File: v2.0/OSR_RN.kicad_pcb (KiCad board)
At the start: 2 copper layers, 63.5 x 43 mm, 76 parts, among them J1 U.FL, J2 I2C, J3 ISP_ATM, J4 ISP_RN, J5 UART, J6 OUT, J7 BAT1, J8 SOL1, J9 USB_B_Micro, Q1 YJL2301F, Q2 BC817, SW1 RESET, U1 ATmega328-AU, U2 CH340E, U3 AP2112K-3.3, U4 MCP73831-2-OT, U5 RN2483, Y1 16MHz

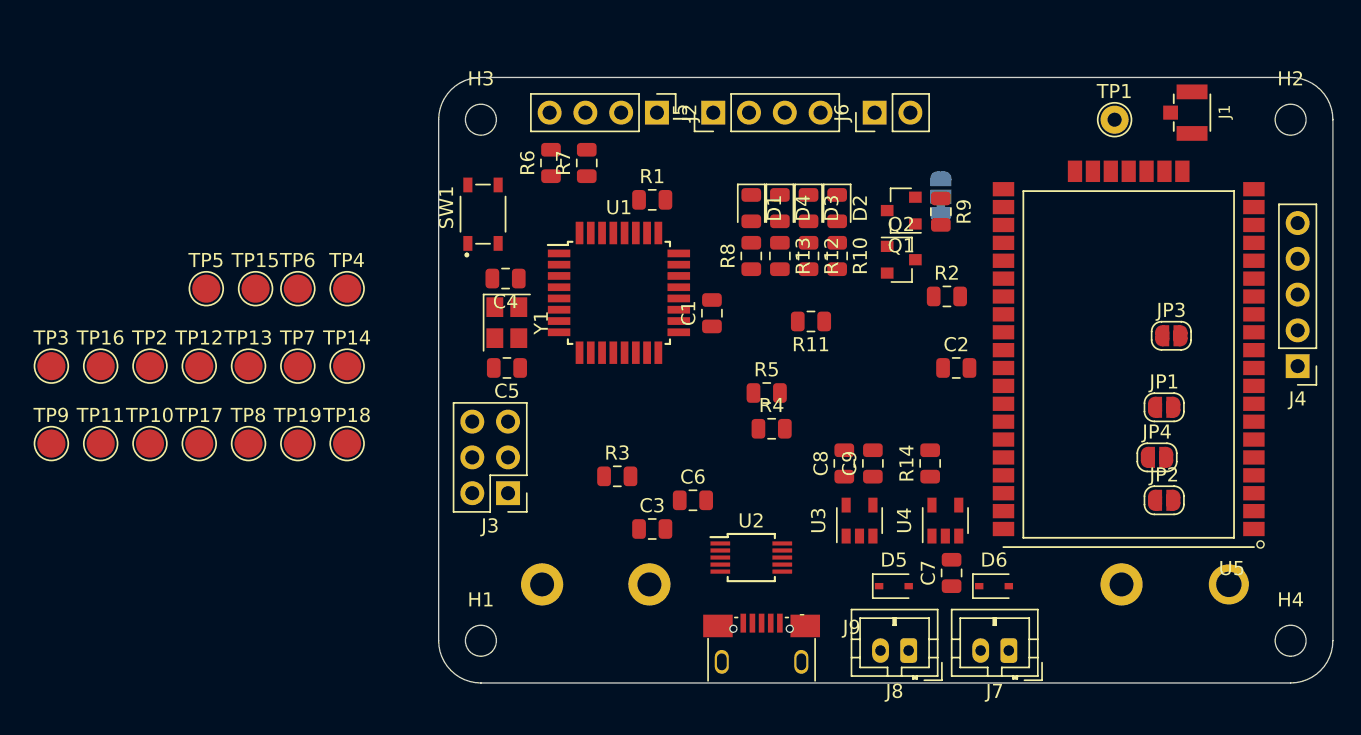
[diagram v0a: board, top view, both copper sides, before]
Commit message: -Zmiany w schemacie: 	-Usunięte połączenia z RN do header'ów, zastąpione TestPoint'ami -Aktualizacja projektu płytki
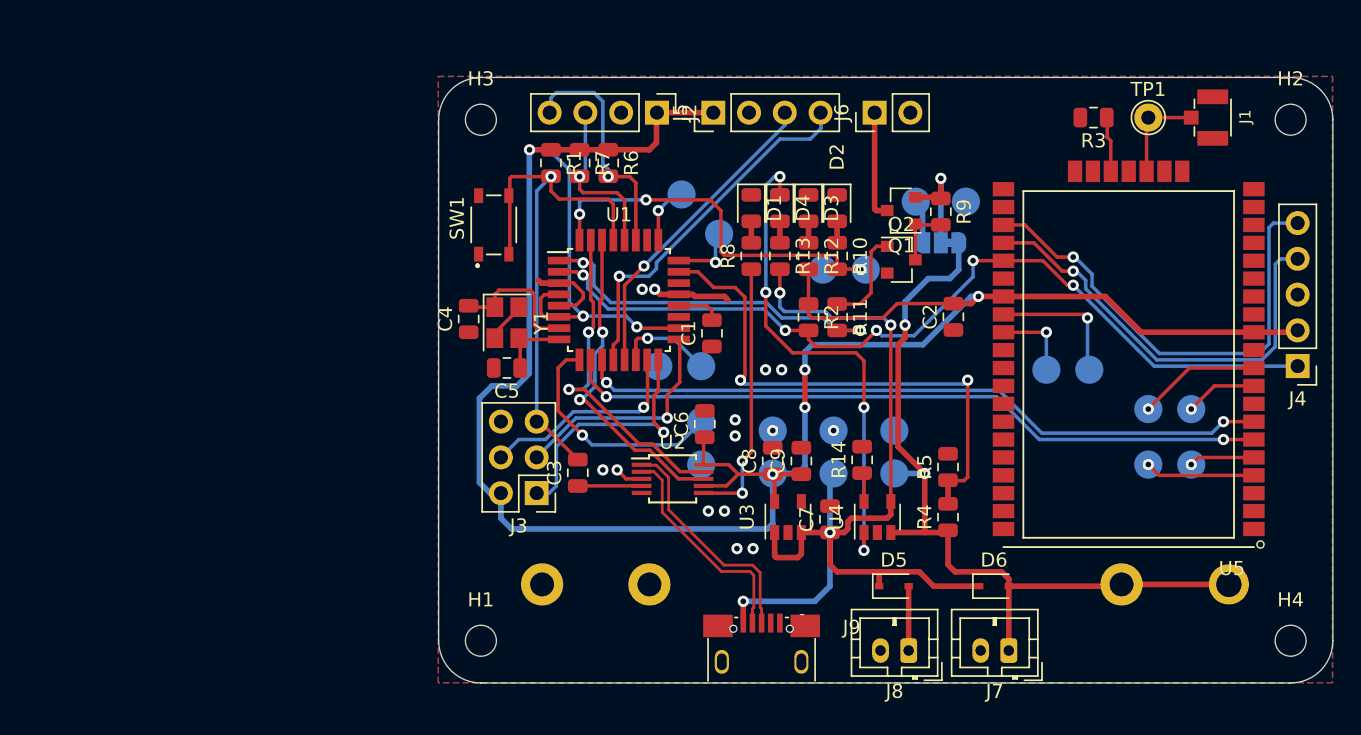
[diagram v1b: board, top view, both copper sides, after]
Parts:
- removed JP1, JP2: RN_LED, Jumper:SolderJumper-2_P1.3mm_Open_RoundedPad1.0x1.5mm
- removed JP3: RX, Jumper:SolderJumper-2_P1.3mm_Open_RoundedPad1.0x1.5mm
- removed JP4: TX, Jumper:SolderJumper-2_P1.3mm_Open_RoundedPad1.0x1.5mm
- added TP20: RN_SDA, TestPoint:TestPoint_Pad_D2.0mm, B.Cu at (167.9, 94.5)
- added TP21: RN_SCL, TestPoint:TestPoint_Pad_D2.0mm, B.Cu at (170.9, 94.5)
- added TP22: RN_RX, TestPoint:TestPoint_Pad_D2.0mm, B.Cu at (167.9, 90.6)
- added TP23: RN_TX, TestPoint:TestPoint_Pad_D2.0mm, B.Cu at (170.9, 90.6)
- TP10, TP11, TP12, TP13, TP14, TP15, TP16, TP17, TP18, TP19, TP2, TP3, TP4, TP5, TP6, TP7, TP8, TP9: moved to B.Cu
- moved TP3 70.7 mm to (160.7, 87.8)
- moved TP2 66.7 mm to (163.7, 87.8)
- moved TP17 57.1 mm to (154.9, 75.8)
- moved TP11 56.4 mm to (149.9, 92.1)
- moved TP9 55.5 mm to (145.5, 92.1)
- moved TP16 54.8 mm to (147.8, 80.6)
- moved TP15 47.3 mm to (151.4, 75.8)
- moved TP5 46.4 mm to (145.5, 95.1)
- moved TP10 44.2 mm to (141.2, 92.1)
- moved R3 42.3 mm to (164.0, 69.8), turned to 180 degrees
- moved TP4 41.0 mm to (149.9, 95.1)
- moved TP19 39.3 mm to (144.8, 80.6)
- moved TP6 36.2 mm to (141.2, 95.1)
- moved TP12 35.9 mm to (136.1, 91.4)
- moved TP13 32.1 mm to (136.1, 87.5)
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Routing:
- net VCC: track 0.00 -> 173.9 mm, vias 0 -> 7
- net VBUS: track 0.00 -> 67.7 mm, vias 0 -> 4
- net D4\RST_RN: track 0.00 -> 61.8 mm, vias 0 -> 5
- net +BATT: track 0.00 -> 58.4 mm, vias 0 -> 2
- net D6\RN_TX: track 0.00 -> 50.3 mm, vias 0 -> 2
- net D7\RN_RX: track 0.00 -> 49.5 mm, vias 0 -> 2
- net RST: track 0.00 -> 38.5 mm, vias 0 -> 1
- net A0: track 0.00 -> 38.0 mm, vias 0 -> 2
- net Net-(D4-Pad1): track 0.00 -> 35.1 mm, vias 0 -> 4
- net PGC_INT: track 0.00 -> 33.8 mm, vias 0 -> 1
- net PGD_INT: track 0.00 -> 31.1 mm, vias 0 -> 1
- net D2\LED: track 0.00 -> 27.0 mm, vias 0 -> 3
- net D8\Rx: track 0.00 -> 26.1 mm, vias 0 -> 1
- net D3\MOSFET: track 0.00 -> 25.9 mm, vias 0 -> 2
- net TxD: track 0.00 -> 23.9 mm, vias 0 -> 2
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- added copper zone on B.Cu, net GND
- added copper zone on F.Cu, net GND

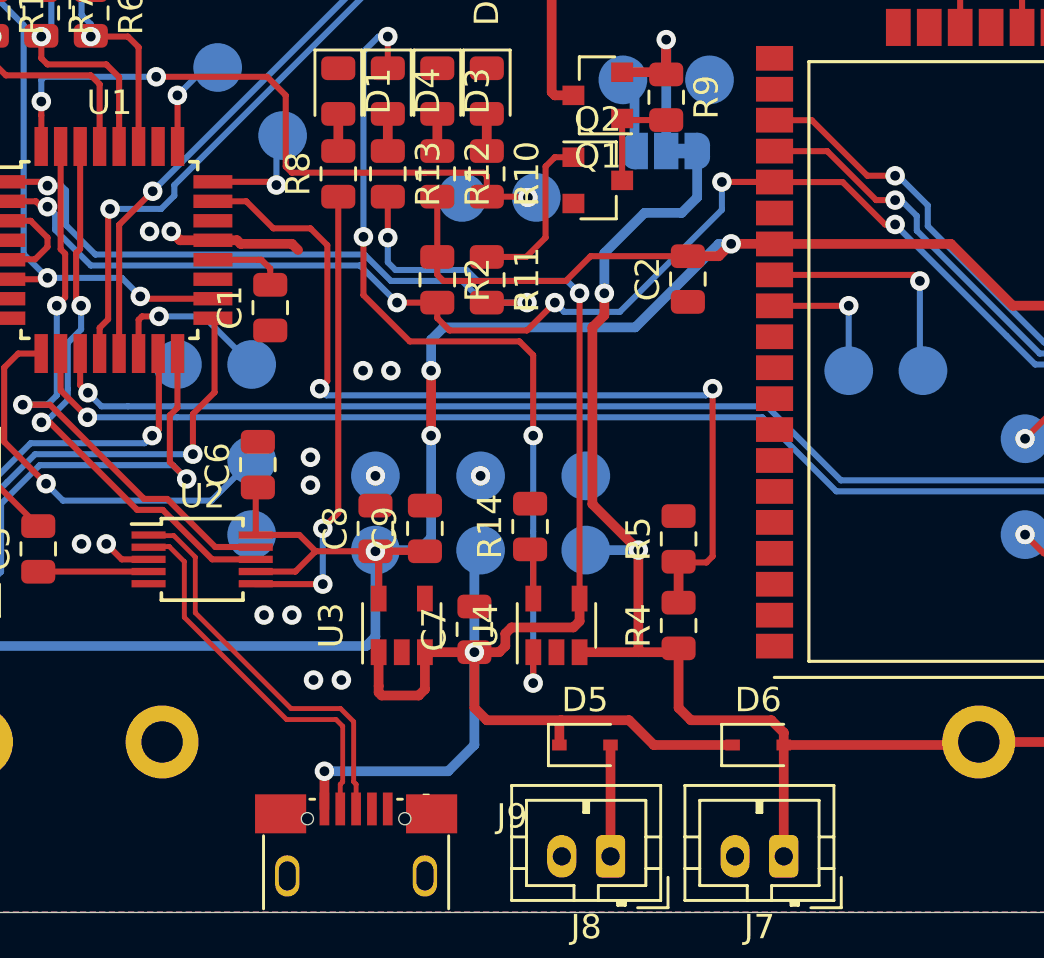
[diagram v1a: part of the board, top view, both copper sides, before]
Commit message: Przeorganizowanie ścieżek.
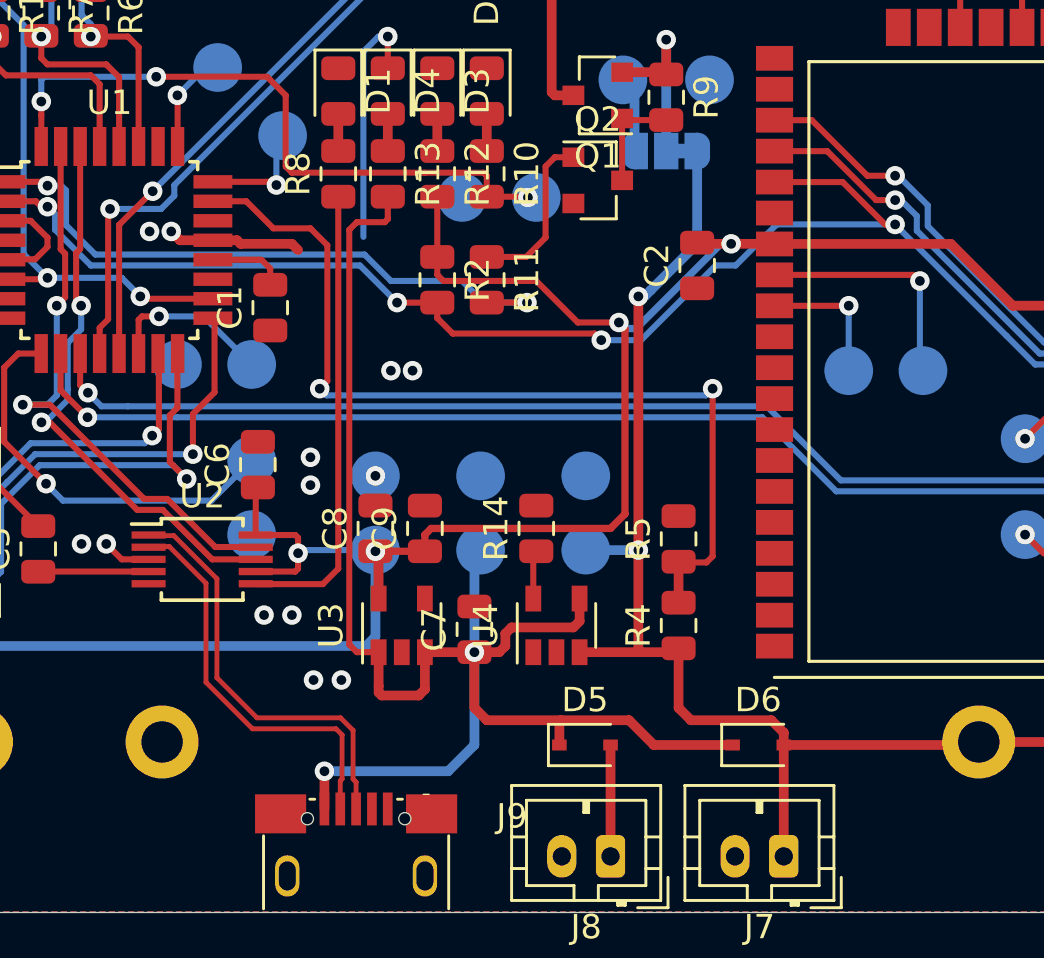
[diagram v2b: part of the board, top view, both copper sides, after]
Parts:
- moved C2 0.67 mm to (154.4, 83.4)
- moved R14 0.27 mm to (147.8, 94.2)
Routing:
- net Net-(D4-Pad1): track 35.1 -> 10.0 mm, vias 4 -> 1
- net D4\RST_RN: track 61.8 -> 65.4 mm, vias 5 -> 4
- net VCC: track 173.9 -> 170.4 mm
- net VBUS: track 67.7 -> 65.1 mm, vias 4 -> 2
- net +BATT: track 58.4 -> 56.1 mm
- net D+: track 16.6 -> 17.4 mm
- net D-: track 15.8 -> 16.6 mm
- net Net-(R8-Pad1): vias 2 -> 0
- net GND: vias 14 -> 13

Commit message: 90%
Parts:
- removed J1: U.FL, U.FL-R-SMT-1_10_:HRS_U.FL-R-SMT-1(10)
- removed J7: BAT1, Connector_JST:JST_PH_B2B-PH-K_1x02_P2.00mm_Vertical
- removed J8: SOL1, Connector_JST:JST_PH_B2B-PH-K_1x02_P2.00mm_Vertical
- removed J9: USB_B_Micro, OSR_BOARD:micro_usb
- added ANT: U.FL, OSR_BOARD:HRS_U.FL-R-SMT-1(10), F.Cu at (172.5, 69.8)
- added BATTERY: BAT1, Connector_JST:JST_PH_S2B-PH-K_1x02_P2.00mm_Horizontal, F.Cu at (158.1, 103.5)
- added PV: SOL1, Connector_JST:JST_PH_S2B-PH-K_1x02_P2.00mm_Horizontal, F.Cu at (151.1, 103.5)
- added Ref**: Val**, OSR_BOARD:OSR_Horizontal_12x29, B.Cu at (160.9, 79.6)
- added USB: USB_B_Micro, OSR_BOARD:WE_629105136821, F.Cu at (140.4, 108.2)
- moved D6 9.97 mm to (147.1, 104.5)
- moved GND 6.10 mm to (139.2, 87.5)
- moved A1 4.87 mm to (136.1, 73.4)
- moved D5 3.75 mm to (136.1, 95.2)
- moved D5 2.81 mm to (147.1, 102.6)
- moved TP7 2.52 mm to (133.1, 73.4)
- moved A_IN 2.41 mm to (163.7, 90.2)
- moved D_OUT 2.41 mm to (160.7, 90.2)
- moved GND 2.41 mm to (136.1, 92.1)
- moved RX 1.09 mm to (166.9, 90.2)
- moved TX 1.09 mm to (169.9, 90.2)
- moved Q1 0.06 mm to (150.4, 76.4)
- renumbered TP14 to A1, J3 to ATM_ISP, TP2 to A_IN, TP13 to D10, TP16 to D2/LED, TP12 to D5, TP3 to D_OUT, TP8 to GND, TP17 to GND, TP18 to GND, TP19 to GND, J2 to I2C, J6 to OUT, SW1 to RESET, U5 to RN2483, J4 to RN_ISP, TP22 to RX, TP21 to SCL, TP20 to SDA, TP23 to TX, J5 to UART, TP5 to VBUS, TP6 to VCC, TP4 to V_BAT, TP15 to V_EXT
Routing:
- net Net-(D4-Pad1): track 10.0 -> 42.5 mm, vias 1 -> 4
- net VBUS: track 65.1 -> 56.1 mm
- net +BATT: track 56.1 -> 64.4 mm
- net VCC: track 170.4 -> 162.8 mm
- net GND: track 16.2 -> 20.6 mm, vias 13 -> 18
- net A1: track 4.44 -> 7.41 mm
- net RST: track 38.5 -> 36.0 mm, vias 1 -> 2
- net A0: track 38.0 -> 39.8 mm
- net A2: track 3.72 -> 5.40 mm
- net Net-(TP3-Pad1): track 5.84 -> 7.25 mm
- net Net-(TP22-Pad1): track 8.70 -> 10.0 mm
- net Net-(D5-Pad2): track 4.57 -> 3.42 mm
- net D2\LED: track 27.0 -> 28.1 mm
- net PGD_INT: track 31.1 -> 32.1 mm
- net Net-(TP23-Pad1): track 5.13 -> 5.99 mm
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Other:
- board text added: "LoRa Dev Board v2"
- board text added: "RN_2483"
- board text added: "VCC"
- board text added: "WWW.OTWARTASIECRZECZY.ORG"

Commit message: 95%
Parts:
- moved Ref** 4.61 mm to (162.7, 83.8), turned to 180 degrees
- renumbered TP7 to A2, D4 to CHG, D2 to LED, D1 to USB, D3 to VCC

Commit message: SCH: -kosmetyka PCB: -Zmiana złącz baterii i panelu fotowoltaicznego na raster 2.5mm (JST). -Zmiana obudowy diod zabezpieczających. -Kosmetyka
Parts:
- D5, D6: footprint Diode_SMD:D_SOD-323 -> Diode_SMD:D_SOD-123
- TP2: renamed from A_IN; value RN_ANALOG_IN -> A_IN
- TP3: renamed from D_OUT; value LED -> D_OUT
- moved D6 18.1 mm to (165.1, 106.6)
- moved D5 1.45 mm to (147.4, 104.0), turned to 90 degrees
- renumbered USB to D1, LED to D2, VCC to D3, CHG to D4, ANT to J1, I2C to J2, ATM_ISP to J3, RN_ISP to J4, UART to J5, OUT to J6, BATTERY to J7, PV to J8, USB to J9, RESET to SW1, D5 to TP12, D10 to TP13, A1 to TP14, V_EXT to TP15, D2/LED to TP16, GND to TP17, GND to TP18, GND to TP19, SDA to TP20, SCL to TP21, RX to TP22, TX to TP23, V_BAT to TP4, VBUS to TP5, VCC to TP6, A2 to TP7, GND to TP8, RN2483 to U5
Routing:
- net VBUS: track 56.1 -> 74.9 mm
- net +BATT: track 64.4 -> 57.0 mm
- net Net-(D5-Pad2): track 3.42 -> 4.28 mm

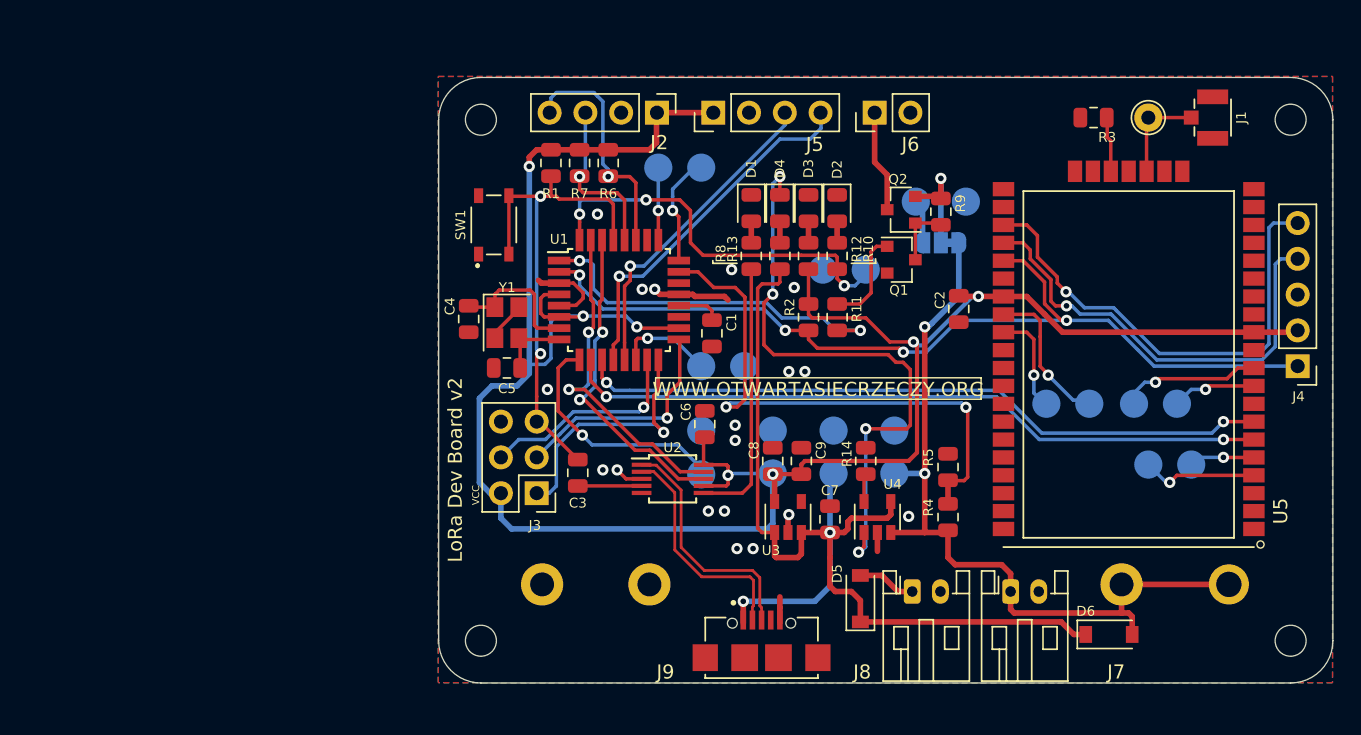
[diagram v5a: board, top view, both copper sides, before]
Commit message: Zmiana złącza USB Zmiana złącz baterii i panelu fotowoltaicznego Dodanie opisów Kosmetyka
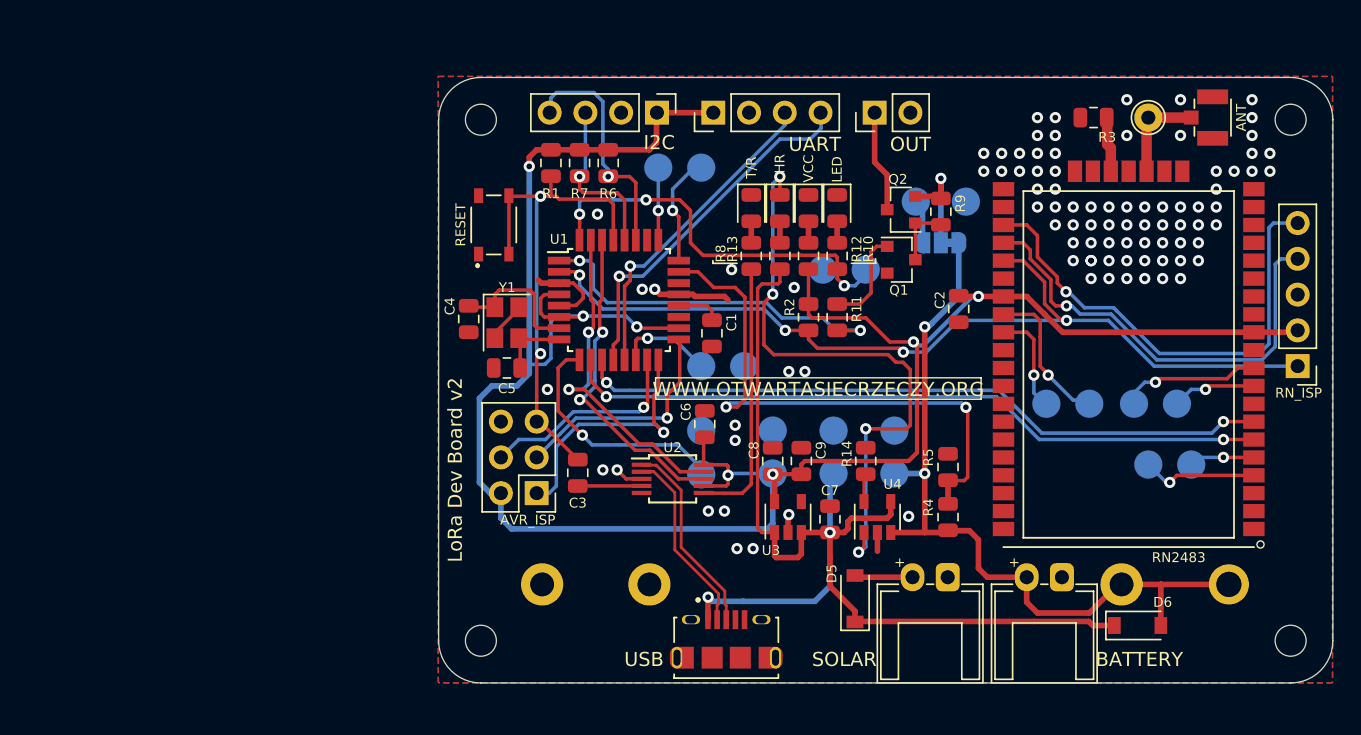
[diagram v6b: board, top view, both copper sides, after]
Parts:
- removed J7: BAT1, Connector_JST:JST_PH_S2B-PH-K_1x02_P2.00mm_Horizontal
- removed J8: SOL1, Connector_JST:JST_PH_S2B-PH-K_1x02_P2.00mm_Horizontal
- removed J9: USB_B_Micro, OSR_BOARD:WE_629105136821
- removed Ref**: Val**, OSR_BOARD:OSR_Horizontal_12x29
- added A1: Logo, OSR_BOARD:OSR_H, B.Cu at (132.1, 81.3)
- added A2: Logo, OSR_BOARD:OSR_V, B.Cu at (164.8, 81.5)
- added BATTERY: BAT1, OSR_BOARD:XH-2AW, F.Cu at (160.5, 100.5)
- added SOLAR: SOL1, OSR_BOARD:XH-2AW, F.Cu at (152.4, 100.5)
- added USB: USB_B_Micro, OSR_BOARD:AMPHENOL_10118194-0001LF, F.Cu at (137.9, 108.2)
- H1, H2, H3, H4: value MountingHole -> M2 Hole
- moved D6 2.13 mm to (167.1, 105.9)
- moved D5 0.38 mm to (147.1, 104.0)
- renumbered TP14 to A1, TP7 to A2, J1 to ANT, J3 to AVR_ISP, TP2 to A_IN, D4 to CHR, TP13 to D10, TP16 to D2/LED, TP12 to D5, TP3 to D_OUT, TP8 to GND, TP17 to GND, TP18 to GND, TP19 to GND, J2 to I2C, D2 to LED, J6 to OUT, SW1 to RESET, U5 to RN2483, J4 to RN_ISP, TP22 to RX, TP21 to SCL, TP20 to SDA, D1 to T/R, TP23 to TX, J5 to UART, TP4 to VBAT, TP5 to VBUS, D3 to VCC, TP6 to VCC, TP15 to VEXT
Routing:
- net VBUS: track 74.9 -> 78.8 mm
- net D+: track 17.4 -> 14.1 mm
- net D-: track 16.6 -> 13.3 mm
- net GND: track 20.6 -> 18.8 mm, vias 18 -> 92
- net +BATT: track 57.0 -> 56.1 mm
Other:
- board text added: "+"
- board text added: "GND"
- board text added: "MISO"
- board text added: "MOSI"
- board text added: "OUT"
- board text added: "PGC"
- board text added: "PGD"
- board text added: "RST"
- board text added: "RX"
- board text added: "SCK"
- board text added: "SCL"
- board text added: "SDA"
- board text added: "TX"

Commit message: v2.2
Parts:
- removed the A1 at (132.1, 81.3)
- removed the A2 at (164.8, 81.5)
- added G***: LOGO, OSR_BOARD:LOGOv2, B.Cu at (132.1, 77.2)
- moved OUT 5.24 mm to (152.4, 66.0)
- moved UART 4.39 mm to (139.7, 66.0)
- moved I2C 3.82 mm to (134.6, 66.0)
- moved A1 3.43 mm to (136.1, 70.0)
- moved A2 3.43 mm to (133.1, 70.0)
- moved AVR_ISP 3.43 mm to (124.5, 93.1)
- moved A_IN 3.43 mm to (163.7, 86.7)
- moved BATTERY 3.43 mm to (160.5, 97.1)
- moved BT1 3.43 mm to (150.5, 99.6)
- moved C3 3.43 mm to (127.4, 91.6)
- moved C4 3.43 mm to (119.6, 80.7)
- moved C5 3.43 mm to (122.3, 84.2)
- moved C6 3.43 mm to (136.4, 88.2)
- moved D10 3.43 mm to (136.1, 84.1)
- moved D2/LED 3.43 mm to (147.8, 77.2)
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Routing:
- net A5\SCL: track 12.0 -> 19.2 mm
- net A4\SDA: track 16.9 -> 11.8 mm
- net D9\Tx: track 22.8 -> 26.3 mm
- net D8\Rx: track 25.9 -> 29.0 mm
- net VCC: track 162.8 -> 165.5 mm
- net Net-(J6-Pad1): track 7.32 -> 8.99 mm
